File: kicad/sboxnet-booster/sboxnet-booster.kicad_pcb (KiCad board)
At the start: 2 copper layers, 70 parts, among them J1 sboxnet-stecker_02x17, J3 Conn_01x02_Male, J4 Conn_01x02_Male, J5 Screw_Terminal_01x04, J6 Screw_Terminal_01x04, J7 Power von externen 15V/4A Net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, SW1 Öffner, U1 L6206PSO-sboxnet, U2 L78L12_SOT89

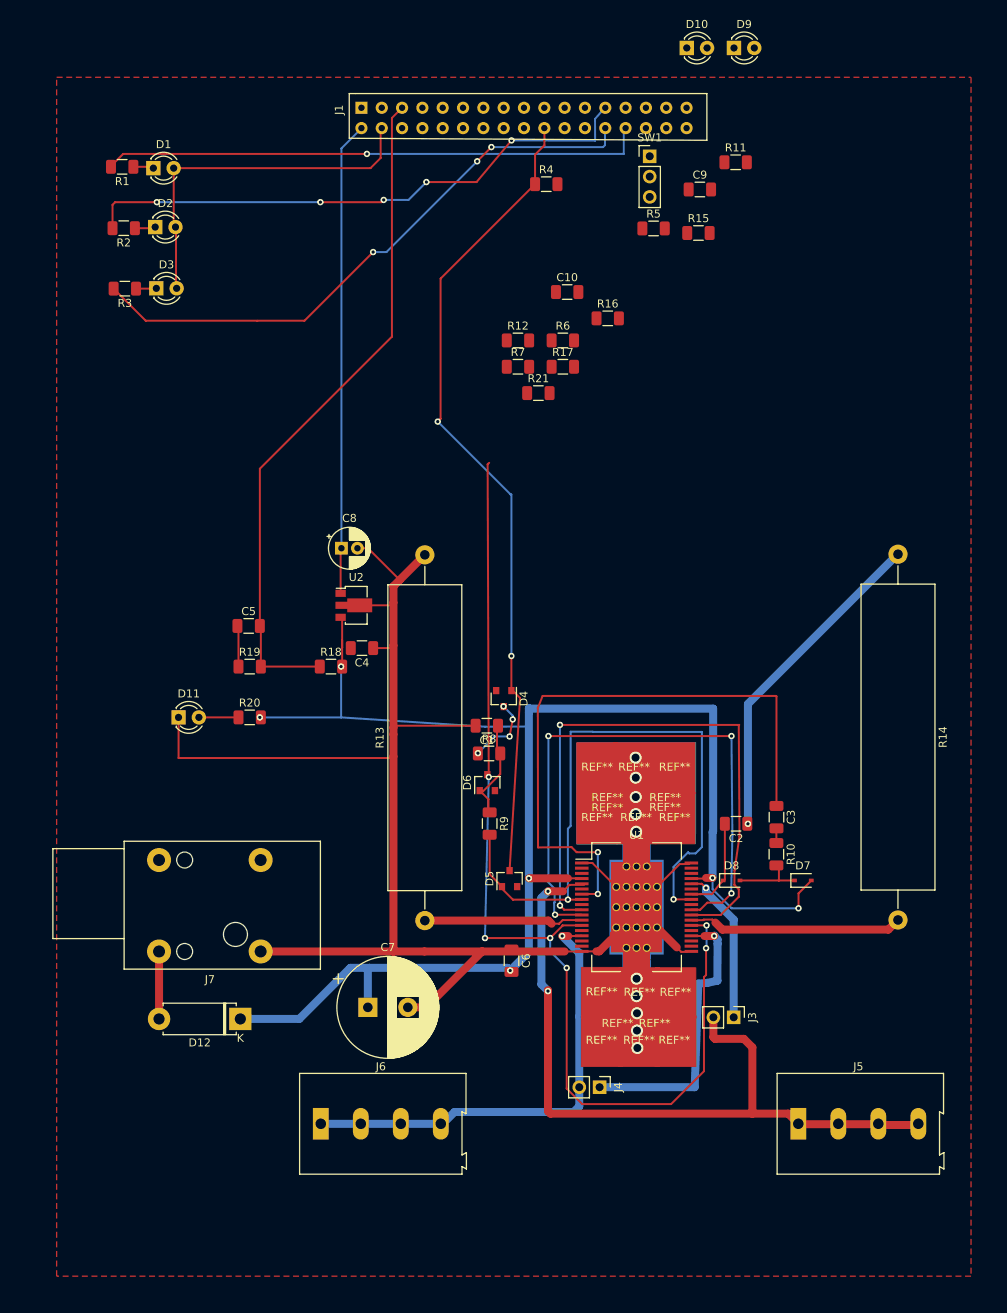
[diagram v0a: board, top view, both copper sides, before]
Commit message: finished booster layout
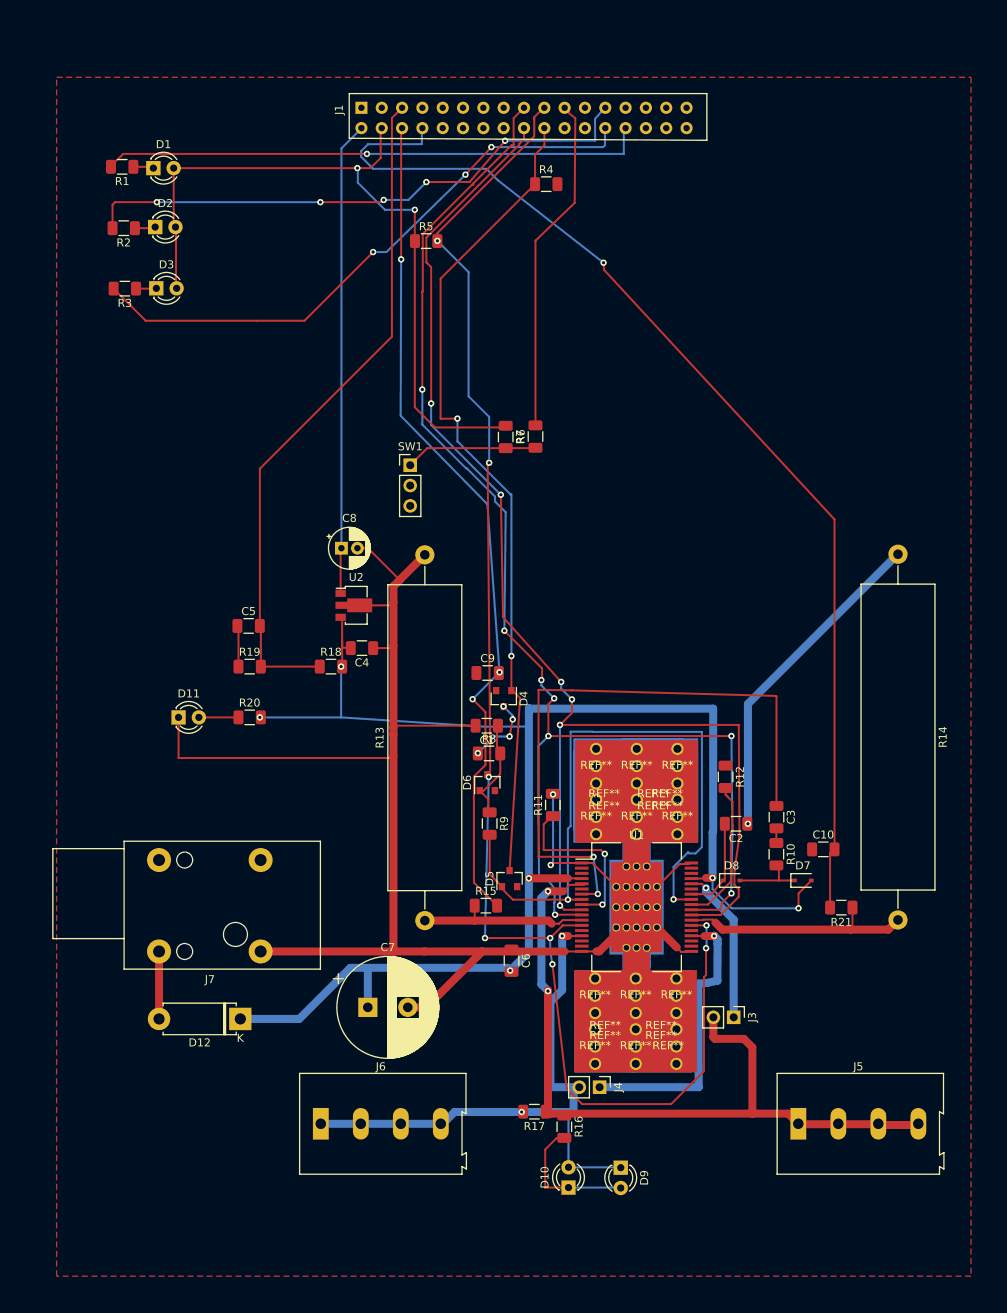
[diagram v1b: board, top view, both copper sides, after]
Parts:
- removed the REF** at (95.5, 143.1)
- removed the REF** at (102.7, 117.4)
- removed the REF** at (93.0, 117.4)
- removed the REF** at (97.8, 117.4)
- removed the REF** at (102.8, 145.2)
- removed the REF** at (93.5, 145.2)
- removed the REF** at (98.2, 145.2)
- removed the REF** at (102.8, 139.2)
- removed the REF** at (93.5, 139.2)
- removed the REF** at (98.2, 139.2)
- removed the REF** at (100.2, 143.1)
- removed the REF** at (101.5, 114.9)
- removed the REF** at (94.2, 114.9)
- removed the REF** at (94.2, 116.2)
- removed the REF** at (101.4, 116.1)
- removed the REF** at (93.0, 111.1)
- removed the REF** at (97.6, 111.1)
- removed the REF** at (102.7, 111.1)
- added REF**: hs_b, sboxnet:heatsink_b, F.Cu at (101.0, 144.7)
- added REF**: hs, sboxnet:heatsink_f, F.Cu at (103.0, 110.9)
- added REF**: hs, sboxnet:heatsink_f, F.Cu at (97.9, 110.9)
- added REF**: hs, sboxnet:heatsink_f, F.Cu at (97.9, 117.2)
- added REF**: hs_b, sboxnet:heatsink_b, F.Cu at (99.9, 114.4)
- added REF**: hs_b, sboxnet:heatsink_b, F.Cu at (93.9, 114.4)
- added REF**: hs_b, sboxnet:heatsink_b, F.Cu at (93.9, 116.0)
- added REF**: hs_b, sboxnet:heatsink_b, F.Cu at (99.9, 116.0)
- added REF**: hs, sboxnet:heatsink_f, F.Cu at (102.9, 145.9)
- added REF**: hs, sboxnet:heatsink_f, F.Cu at (102.9, 139.6)
- added REF**: hs, sboxnet:heatsink_f, F.Cu at (92.7, 145.9)
- added REF**: hs_b, sboxnet:heatsink_b, F.Cu at (94.0, 144.7)
- added REF**: hs, sboxnet:heatsink_f, F.Cu at (92.7, 139.6)
- added REF**: hs, sboxnet:heatsink_f, F.Cu at (97.8, 145.9)
- added REF**: hs, sboxnet:heatsink_f, F.Cu at (97.8, 139.6)
- added REF**: hs_b, sboxnet:heatsink_b, F.Cu at (101.0, 143.4)
- added REF**: hs_b, sboxnet:heatsink_b, F.Cu at (94.0, 143.4)
- added REF**: hs_b, sboxnet:heatsink_b, F.Cu at (101.7, 116.0)
- added REF**: hs_b, sboxnet:heatsink_b, F.Cu at (101.7, 114.4)
- added REF**: hs, sboxnet:heatsink_f, F.Cu at (92.8, 110.9)
- added REF**: hs, sboxnet:heatsink_f, F.Cu at (92.8, 117.2)
- added REF**: hs, sboxnet:heatsink_f, F.Cu at (103.0, 117.2)
- moved D10 143.2 mm to (89.4, 164.2), turned to 90 degrees
- moved D9 140.7 mm to (95.9, 161.7), turned to 270 degrees
- moved R16 101.2 mm to (88.9, 156.6), turned to 270 degrees
- moved R17 93.2 mm to (85.1, 154.7), turned to 180 degrees
- moved R15 88.2 mm to (79.1, 128.9)
- moved R11 83.5 mm to (87.4, 116.4), turned to 90 degrees
- moved C10 76.7 mm to (121.2, 121.9)
- moved R21 74.6 mm to (123.5, 129.2), turned to 180 degrees
- moved C9 66.0 mm to (79.3, 99.9)
- moved R12 60.4 mm to (109.0, 112.8), turned to 270 degrees
- moved SW1 48.9 mm to (69.6, 73.9)
- moved R5 28.5 mm to (71.6, 45.9)
- moved R6 12.5 mm to (85.3, 70.3), turned to 90 degrees
- moved R7 8.91 mm to (81.5, 70.4), turned to 270 degrees
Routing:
- net PA2: track 0.00 -> 137.9 mm, vias 0 -> 1
- net PA0: track 0.00 -> 105.9 mm, vias 0 -> 3
- net IN2: track 74.6 -> 167.8 mm, vias 4 -> 8
- net IN1: track 76.6 -> 164.2 mm, vias 2 -> 6
- net PC3: track 131.9 -> 183.6 mm, vias 6 -> 8
- net +3V3: track 44.9 -> 92.3 mm, vias 0 -> 2
- net PC5: track 0.00 -> 42.3 mm
- net Net-(R11-Pad1): track 0.00 -> 21.8 mm, vias 0 -> 2
- net Net-(R12-Pad2): track 0.00 -> 18.3 mm
- net Net-(D10-Pad1): track 0.00 -> 17.5 mm
- net OUT1a: track 57.3 -> 74.3 mm, vias 1 -> 2
- net Net-(R6-Pad1): track 0.00 -> 16.6 mm
- net GND: track 275.2 -> 291.7 mm, vias 1 -> 3
- net Net-(R14-Pad2): track 26.9 -> 29.7 mm
- net Net-(R13-Pad1): track 19.3 -> 21.1 mm
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
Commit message: sboxnet booster finished
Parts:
- moved R1 53.7 mm to (32.9, 90.3)
- moved D1 53.5 mm to (38.4, 90.3)
- moved R4 40.5 mm to (88.5, 79.2), turned to 270 degrees
- moved D2 38.8 mm to (38.4, 83.0)
- moved R2 38.8 mm to (32.8, 83.0)
- moved J1 38.2 mm to (58.4, 69.8)
- moved SW1 37.0 mm to (39.9, 96.0)
- moved R5 35.5 mm to (68.6, 81.2)
- moved D3 23.7 mm to (38.5, 75.5)
- moved R3 23.7 mm to (32.6, 75.5)
- moved R6 8.94 mm to (85.3, 79.2)
- moved R7 8.91 mm to (81.7, 79.3)
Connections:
- R1 pad 2: PD2 -> PD0
- R3 pad 2: PD0 -> PD2
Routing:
- net IN2: track 167.8 -> 122.6 mm
- net Net-(R6-Pad1): track 16.6 -> 58.8 mm, vias 0 -> 1
- net PA2: track 137.9 -> 95.8 mm, vias 1 -> 3
- net IN1: track 164.2 -> 123.5 mm, vias 6 -> 5
- net PA1: track 84.8 -> 45.4 mm, vias 0 -> 1
- net +12V: track 58.9 -> 20.0 mm
- net PA0: track 105.9 -> 68.5 mm, vias 3 -> 1
- net PC2: track 103.7 -> 69.4 mm, vias 2 -> 4
- net PC5: track 42.3 -> 13.4 mm, vias 0 -> 1
- net PC3: track 183.6 -> 196.3 mm, vias 8 -> 10
- net PD0: track 74.2 -> 69.6 mm, vias 3 -> 1
- net PD1: track 71.4 -> 73.7 mm, vias 5 -> 2
- net Net-(D3-Pad1): track 2.69 -> 4.72 mm
- net Net-(D1-Pad1): track 2.42 -> 4.15 mm
- net Net-(D2-Pad1): track 2.71 -> 4.22 mm
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- added copper zone on B.Cu, net GND
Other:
- board outline added: 114.3 x 110.5 mm

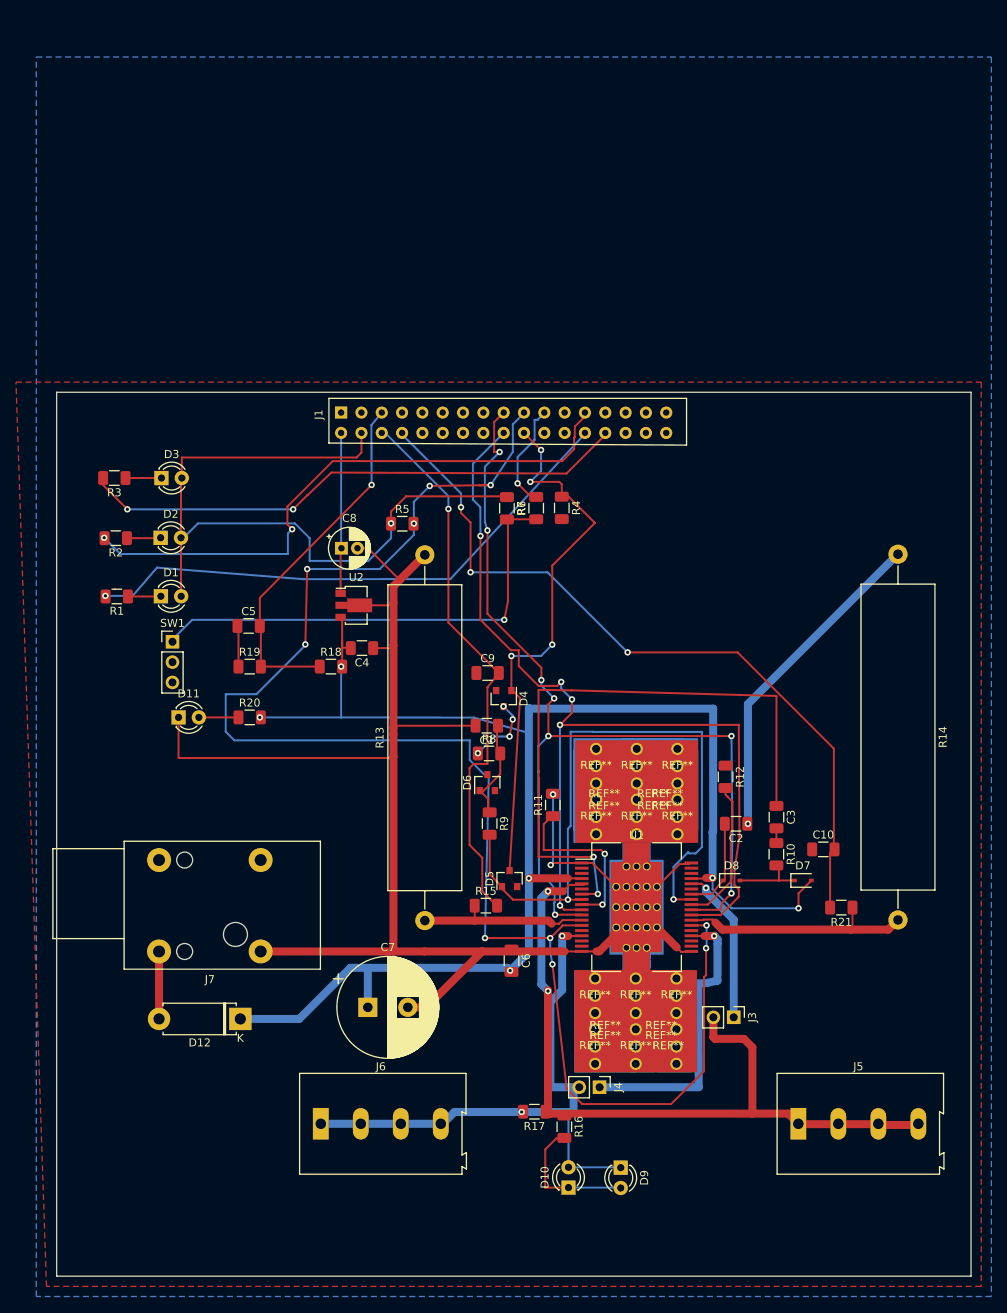
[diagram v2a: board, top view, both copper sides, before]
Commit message: booster DCC Input
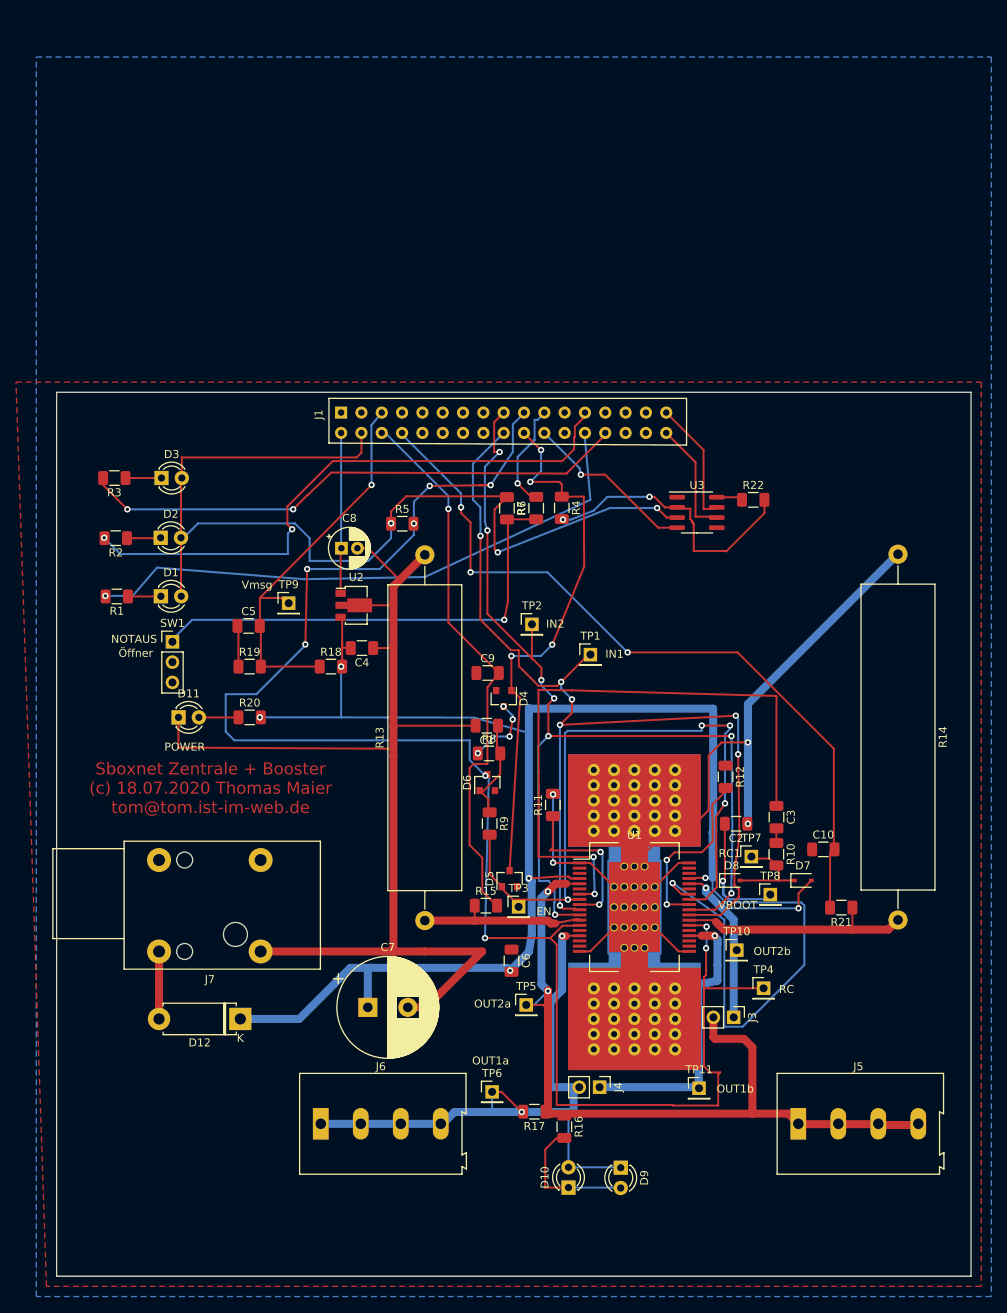
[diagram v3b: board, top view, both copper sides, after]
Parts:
- removed REF** (x10): hs_b, sboxnet:heatsink_b
- removed REF** (x12): hs, sboxnet:heatsink_f
- added R22: 0, Resistor_SMD:R_1206_3216Metric, F.Cu at (112.5, 78.2)
- added TP1: TestPoint, Connector_PinHeader_2.54mm:PinHeader_1x01_P2.54mm_Vertical, F.Cu at (92.1, 97.6)
- added TP10: TestPoint, Connector_PinHeader_2.54mm:PinHeader_1x01_P2.54mm_Vertical, F.Cu at (110.4, 134.5)
- added TP11: TestPoint, Connector_PinHeader_2.54mm:PinHeader_1x01_P2.54mm_Vertical, F.Cu at (105.7, 151.8)
- added TP2: TestPoint, Connector_PinHeader_2.54mm:PinHeader_1x01_P2.54mm_Vertical, F.Cu at (84.8, 93.8)
- added TP3: TestPoint, Connector_PinHeader_2.54mm:PinHeader_1x01_P2.54mm_Vertical, F.Cu at (83.1, 129.1)
- added TP4: TestPoint, Connector_PinHeader_2.54mm:PinHeader_1x01_P2.54mm_Vertical, F.Cu at (113.8, 139.3)
- added TP5: TestPoint, Connector_PinHeader_2.54mm:PinHeader_1x01_P2.54mm_Vertical, F.Cu at (84.1, 141.4)
- added TP6: TestPoint, Connector_PinHeader_2.54mm:PinHeader_1x01_P2.54mm_Vertical, F.Cu at (79.8, 152.2)
- added TP7: TestPoint, Connector_PinHeader_2.54mm:PinHeader_1x01_P2.54mm_Vertical, F.Cu at (112.2, 122.8)
- added TP8: TestPoint, Connector_PinHeader_2.54mm:PinHeader_1x01_P2.54mm_Vertical, F.Cu at (114.6, 127.6)
- added TP9: TestPoint, Connector_PinHeader_2.54mm:PinHeader_1x01_P2.54mm_Vertical, F.Cu at (54.4, 91.1)
- added U3: SN65HVD230, Package_SO:SOIC-8_3.9x4.9mm_P1.27mm, F.Cu at (105.4, 79.8)
- U1: footprint Package_SO:HSOP-36-1EP_11.0x15.9mm_P0.65mm_SlugDown_ThermalVias -> sboxnet:HSOP-36-1EP_11.0x15.9mm_P0.65mm_SlugDown_ThermalVias
- moved U1 0.27 mm to (97.6, 129.1)
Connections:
- J1 pad 21: Net-(J1-Pad21) -> DCC_IN
- J1 pad 33: Net-(J1-Pad33) -> DCC_A
- J1 pad 34: Net-(J1-Pad34) -> DCC_B
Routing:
- net VBOOT: track 11.8 -> 72.9 mm, vias 0 -> 2
- net +3V3: track 93.0 -> 124.8 mm, vias 1 -> 3
- net DCC_IN: track 0.00 -> 21.8 mm, vias 0 -> 1
- net PC3: track 196.3 -> 212.5 mm, vias 10 -> 9
- net DCC_B: track 0.00 -> 15.7 mm
- net DCC_A: track 0.00 -> 14.7 mm
- net Net-(R13-Pad1): track 21.1 -> 31.6 mm
- net OUT1a: track 74.3 -> 81.4 mm
- net IN1: track 123.5 -> 129.5 mm, vias 5 -> 7
- net OUT2a: track 96.0 -> 101.9 mm
- net GND: track 291.7 -> 297.6 mm, vias 3 -> 6
- net EN: track 80.9 -> 85.4 mm, vias 2 -> 4
- net Net-(R12-Pad2): track 18.3 -> 22.4 mm, vias 0 -> 2
- net IN2: track 122.6 -> 126.6 mm
- net PA1: track 45.4 -> 49.3 mm
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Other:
- board text added: "EN"
- board text added: "IN1"
- board text added: "IN2"
- board text added: "NOTAUS"
- board text added: "OUT1a"
- board text added: "OUT1b"
- board text added: "OUT2a"
- board text added: "OUT2b"
- board text added: "POWER"
- board text added: "RC"
- board text added: "RC1"
- board text added: "Sboxnet Zentrale + Booster (c) 18.07.2020 Thomas Maier tom@tom.ist-im-web.de"
- board text added: "VBOOT"
- board text added: "Vmsg"
- board text added: "Öffner"

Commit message: plot pcbs
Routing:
- net Net-(R11-Pad1): track 20.1 -> 19.6 mm
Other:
- board text added: "Sboxnet Booster (c) 18.07.2020 Thomas Maier tom@tom.ist-im-web.de"
- board text removed: "Sboxnet Zentrale + Booster (c) 18.07.2020 Thomas Maier tom@tom.ist-im-web.de"

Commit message: booster cleanup, sboxnet-booster add on led
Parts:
- added D13: LED, LED_THT:LED_D3.0mm, F.Cu at (38.5, 68.2)
- added R23: 680, Resistor_SMD:R_1206_3216Metric, F.Cu at (32.7, 68.2)
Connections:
- net DCC_IN renamed Net-(J1-Pad21)
- J1 pad 28: Net-(J1-Pad28) -> PD3
- SW1 pad 2: Net-(SW1-Pad2) -> GND
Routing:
- net PD3: track 0.00 -> 65.9 mm
- net +3V3: track 124.8 -> 129.7 mm
- net Net-(D13-Pad1): track 0.00 -> 4.42 mm
